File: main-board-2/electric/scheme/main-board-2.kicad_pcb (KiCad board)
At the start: 2 copper layers, 85 x 56 mm, 125 parts, among them K1 power-switch, K2 usb-power-switch, P1 batt, P10 rst, P11 screw-1, P13 screw-2, P14 gpio-big, P15 gpio-small, P16 moto-1, P17 moto-2, P2 CONN_4, P3 trigger-btn, P4 CONN_3X2, P5 reg-short-to-gnd-1, P6 reg-short-to-gnd-2, P7 bootloader, P8 cross board conn, P9 rst, Q1 IRLML2244, Q10 IRLML2244, Q11 sot223, Q12 bc857, Q13 irlml2244, Q2 BC847, Q3 IRLML2244, Q4 IRLML2244, Q5 BC847, Q6 BC847, Q7 BC847, Q8 BC847, Q9 IRLML2244, U1 LM317AEMP, U2 LM317AT, U3 LM317AEMP, U4 LM317AT, U5 LM293, U6 L298, U7 MINI-USB-B, X1 8MHz

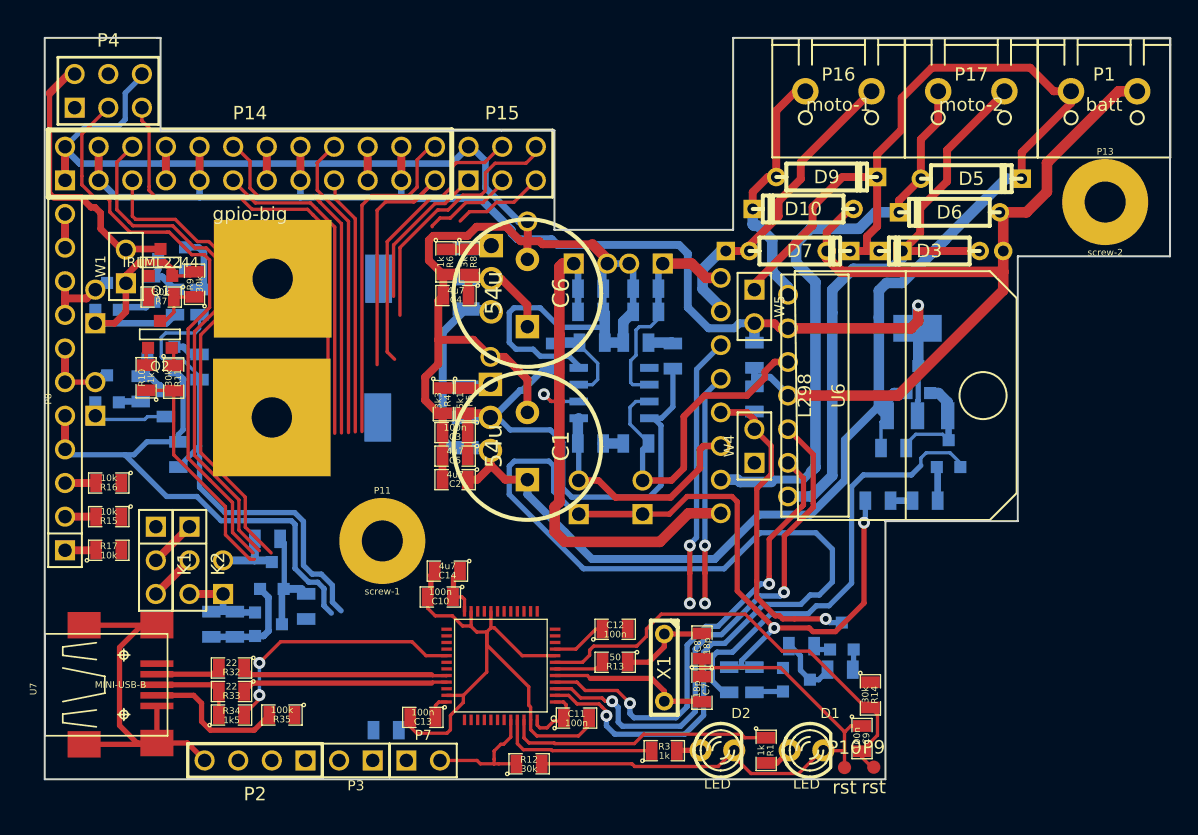
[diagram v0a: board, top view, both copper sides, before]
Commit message: Routing rx and tx...
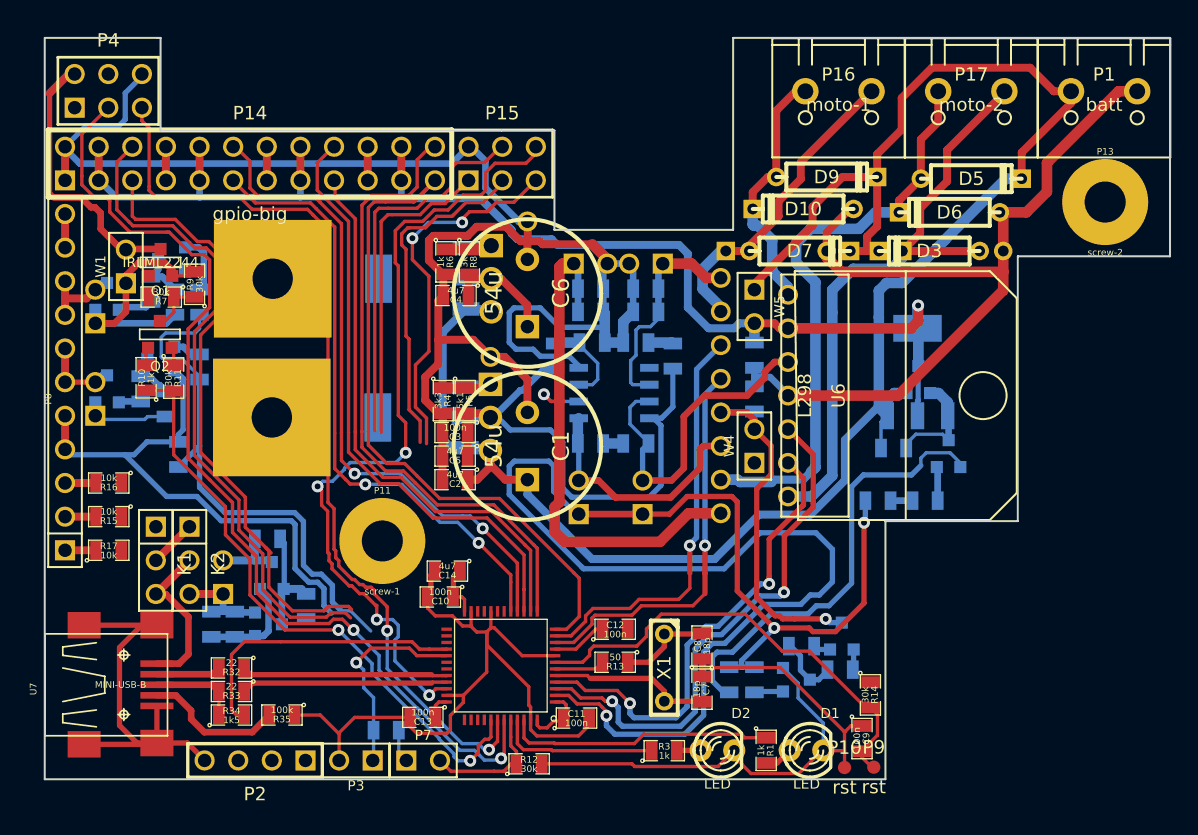
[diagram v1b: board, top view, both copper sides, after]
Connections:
- stm1 pad 10: /gpio-1 -> /in-moto2
- stm1 pad 11: /gpio-2 -> /in-moto1
- stm1 pad 12: /gpio-3 -> /gpio-4
- stm1 pad 13: /gpio-4 -> /gpio-8
- stm1 pad 14: /gpio-5 -> /gpio-3
- stm1 pad 15: /gpio-6 -> /gpio-7
- stm1 pad 16: /gpio-7 -> /gpio-6
- stm1 pad 17: /gpio-8 -> /gpio-2
- stm1 pad 26: /in-moto2 -> /gpio-5
- stm1 pad 27: /in-moto1 -> /gpio-1
- stm1 pad 28: /trigger-button -> /usb-connected
- stm1 pad 29: /usb-connected -> /trigger-button
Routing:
- net /swd-io: track 19.6 -> 61.2 mm, vias 0 -> 4
- net /scl-rpi: track 36.5 -> 69.5 mm, vias 0 -> 2
- net /gpio-4: track 19.2 -> 51.3 mm
- net /sda-rpi: track 44.0 -> 74.8 mm, vias 0 -> 2
- net /rpi-pwr-en: track 17.5 -> 46.2 mm, vias 0 -> 2
- net /gpio-8: track 25.6 -> 48.0 mm
- net /gpio-3: track 19.7 -> 42.0 mm
- net /gpio-6: track 27.6 -> 49.8 mm, vias 0 -> 2
- net /gpio-7: track 23.1 -> 45.3 mm
- net /gpio-2: track 24.7 -> 46.8 mm, vias 0 -> 2
- net /tx: track 6.99 -> 28.1 mm, vias 0 -> 2
- net GND: track 378.1 -> 397.4 mm
- net /rx: track 6.91 -> 25.7 mm
- net /trigger-button: track 0.00 -> 15.5 mm, vias 0 -> 1
- net /in-moto2: track 17.5 -> 29.8 mm, vias 2 -> 1
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
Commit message: Routing...
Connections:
- stm1 pad 18: /addon-pwr-en -> /gpio-1
- stm1 pad 26: /gpio-5 -> /addon-pwr-en
- stm1 pad 27: /gpio-1 -> /gpio-5
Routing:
- net /rx: track 25.7 -> 57.1 mm, vias 0 -> 2
- net /tx: track 28.1 -> 57.9 mm, vias 2 -> 4
- net GND: track 397.4 -> 423.6 mm
- net /gpio-5: track 49.9 -> 59.5 mm, vias 0 -> 2
- net /gpio-1: track 46.4 -> 41.7 mm
- net /addon-pwr-en: track 40.0 -> 35.8 mm
- net /scl-rpi: track 69.5 -> 71.3 mm
- net /sda-rpi: track 74.8 -> 74.3 mm

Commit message: Routing...
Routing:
- net /swd-clk: track 29.0 -> 70.4 mm, vias 0 -> 2
- net /gpio-9: track 23.8 -> 44.9 mm, vias 0 -> 1
- net /addon-pwr-en: track 35.8 -> 45.1 mm, vias 0 -> 1
- net /gpio-2: track 46.8 -> 50.0 mm
- net /trigger-button: track 15.8 -> 18.6 mm
- net GND: track 423.6 -> 421.3 mm
- net /rx: track 57.1 -> 59.2 mm
- net /swd-io: track 60.7 -> 62.7 mm
- net /gpio-5: track 59.5 -> 57.9 mm
- net /tx: track 57.9 -> 59.5 mm
- net /gpio-6: track 49.8 -> 51.4 mm
- net /sda-rpi: track 74.3 -> 75.6 mm
- net /rpi-pwr-en: track 46.2 -> 47.0 mm

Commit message: Routing...
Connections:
- stm1 pad 12: /gpio-4 -> /gpio-9
- stm1 pad 13: /gpio-8 -> /gpio-4
- stm1 pad 14: /gpio-3 -> /gpio-8
- stm1 pad 15: /gpio-7 -> /gpio-3
- stm1 pad 16: /gpio-6 -> /gpio-7
- stm1 pad 17: /gpio-2 -> /gpio-6
- stm1 pad 18: /gpio-1 -> /gpio-2
- stm1 pad 25: /gpio-9 -> /gpio-1
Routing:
- net /sda-int: track 2.35 -> 13.6 mm
- net /gpio-1: track 41.7 -> 52.5 mm, vias 0 -> 2
- net /scl-int: track 2.35 -> 11.6 mm
- net /addon-trigger: track 0.00 -> 8.70 mm
- net /gpio-4: track 51.3 -> 47.4 mm
- net /gpio-9: track 44.9 -> 47.7 mm, vias 1 -> 2
- net /addon-vdd: track 5.93 -> 8.47 mm
- net /addon-pwr-en: track 45.1 -> 46.0 mm

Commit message: Routing...
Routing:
- net GND: track 421.3 -> 433.4 mm
- net /trigger-button: track 18.6 -> 29.9 mm
- net /usb-connected: track 22.5 -> 23.5 mm

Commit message: Routing...
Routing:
- net /scl-rpi: track 71.5 -> 76.5 mm
- net /swd-io: track 63.1 -> 67.5 mm
- net GND: track 433.4 -> 430.6 mm
- net /addon-pwr-en: track 45.8 -> 48.2 mm
- net /rpi-pwr-en: track 47.0 -> 49.0 mm
- net /sda-rpi: track 75.6 -> 77.5 mm
- net /gpio-5: track 57.9 -> 59.1 mm

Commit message: Routing...
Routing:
- net VDD: track 66.1 -> 164.8 mm, vias 0 -> 6
- net GND: track 430.6 -> 512.2 mm, vias 0 -> 1
- net /batt+: track 148.1 -> 187.4 mm
- net /addon-trigger: track 8.70 -> 44.4 mm, vias 0 -> 4
- net /scl-int: track 11.6 -> 46.8 mm, vias 0 -> 4
- net /sda-int: track 13.6 -> 45.5 mm, vias 0 -> 4
- net /moto-en: track 117.9 -> 103.1 mm, vias 3 -> 2
- net /swd-clk: track 70.0 -> 63.5 mm
- net N-0000031: track 24.4 -> 28.1 mm
- net N-0000030: track 33.8 -> 31.0 mm
- net /tx: track 59.5 -> 61.5 mm
- net /rx: track 59.5 -> 61.5 mm
- net /in-moto3: track 40.6 -> 38.7 mm
- net /addon-pwr-en: track 48.2 -> 49.9 mm
- net /led1: track 20.2 -> 21.8 mm
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
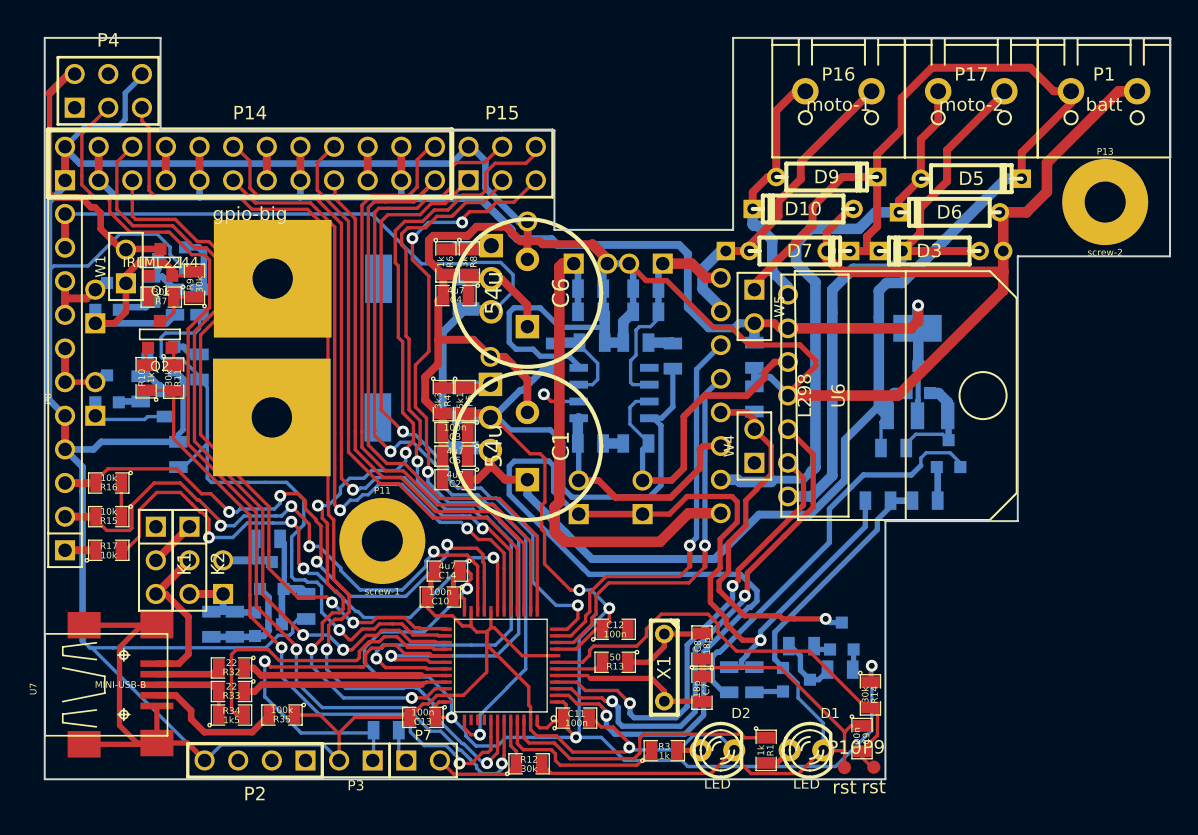
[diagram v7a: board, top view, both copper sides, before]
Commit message: Routing. It turnes out it is very nontrivial to route with horizontal TO-220. I'm going to change to vertical TO-220.
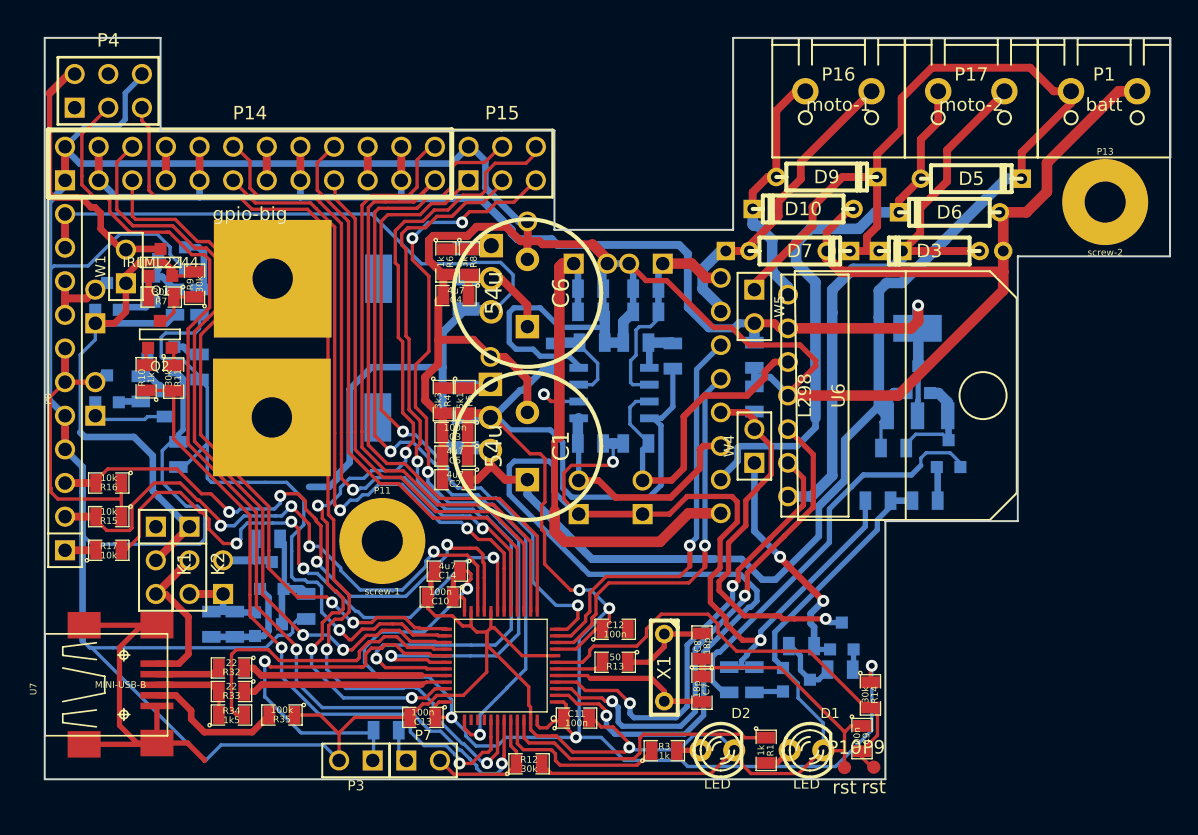
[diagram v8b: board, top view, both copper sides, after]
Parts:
- removed P2: CONN_4, PIN_ARRAY_4x1
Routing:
- net /+5V: track 24.0 -> 62.0 mm, vias 0 -> 2
- net /batt+: track 187.4 -> 207.3 mm
- net /addon-vdd: track 8.47 -> 22.8 mm
- net GND: track 512.2 -> 523.1 mm
- net /moto-en: track 103.1 -> 112.1 mm, vias 2 -> 3
- net N-0000045: track 1.87 -> 3.80 mm
- net N-0000024: track 0.00 -> 1.61 mm
- net /out3: track 44.3 -> 43.1 mm
